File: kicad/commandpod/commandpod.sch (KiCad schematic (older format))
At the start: 3 parts

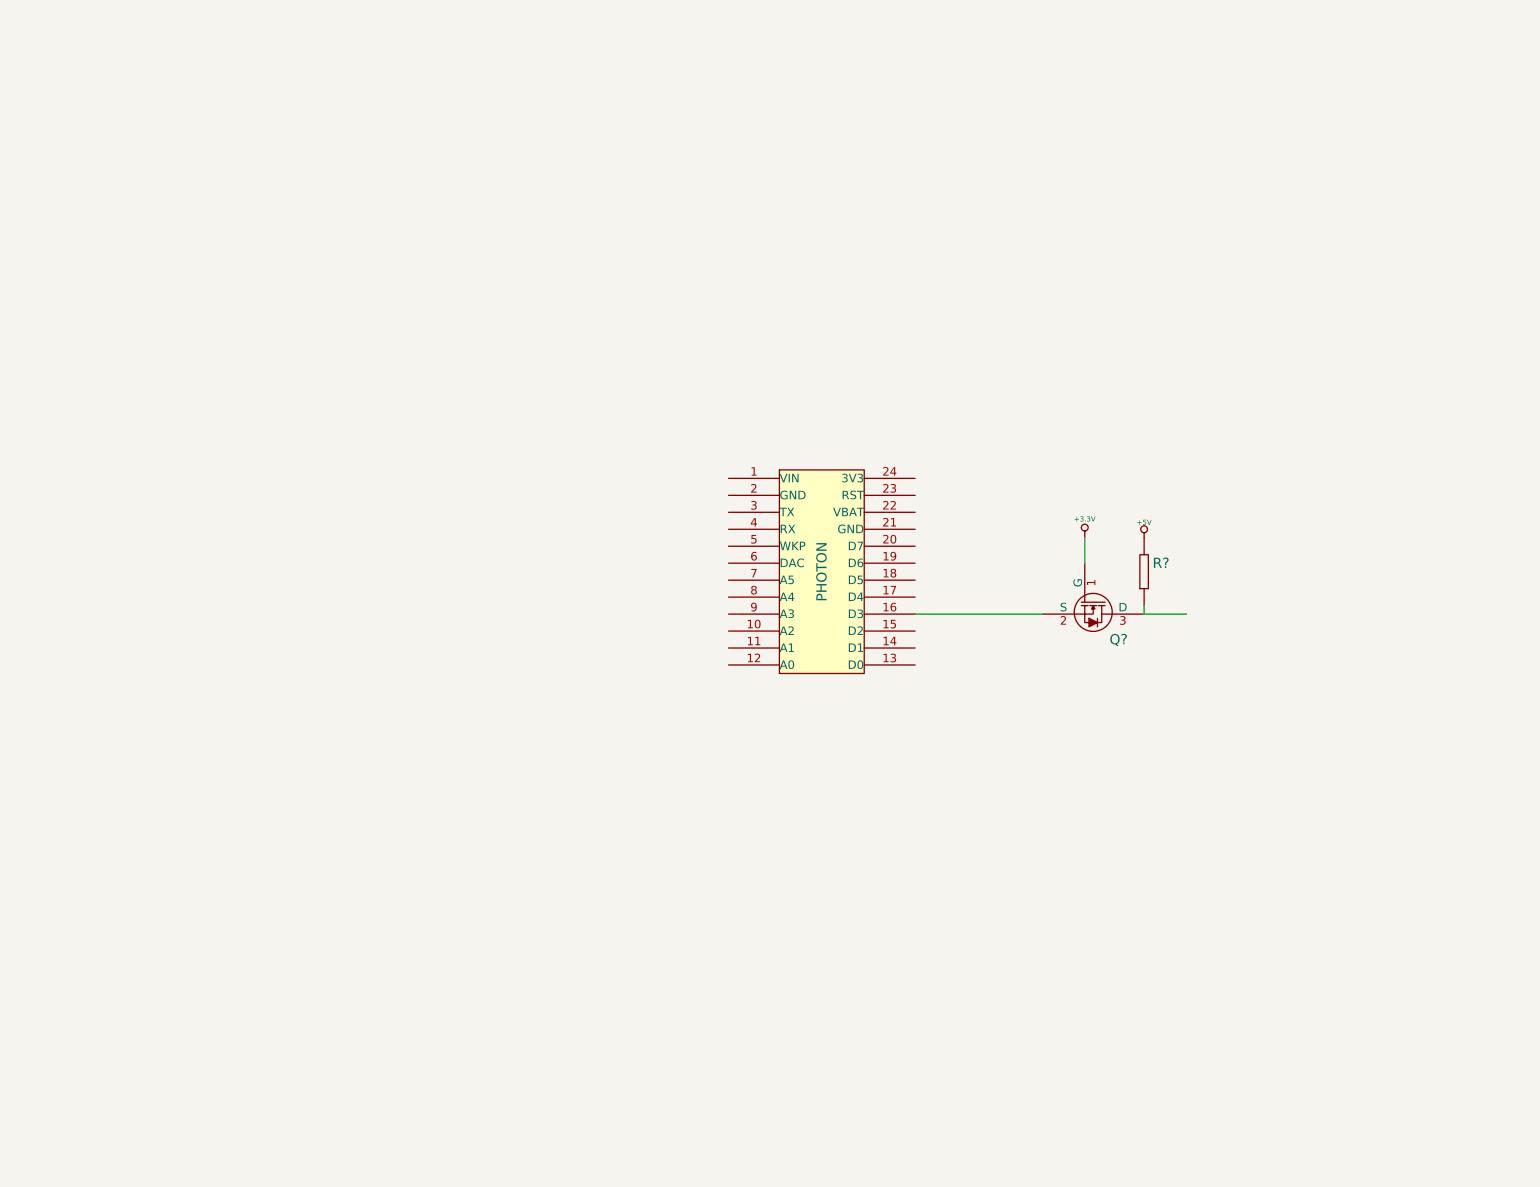
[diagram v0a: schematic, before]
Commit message: Added SPDT switch, put in ir emitter with power switch
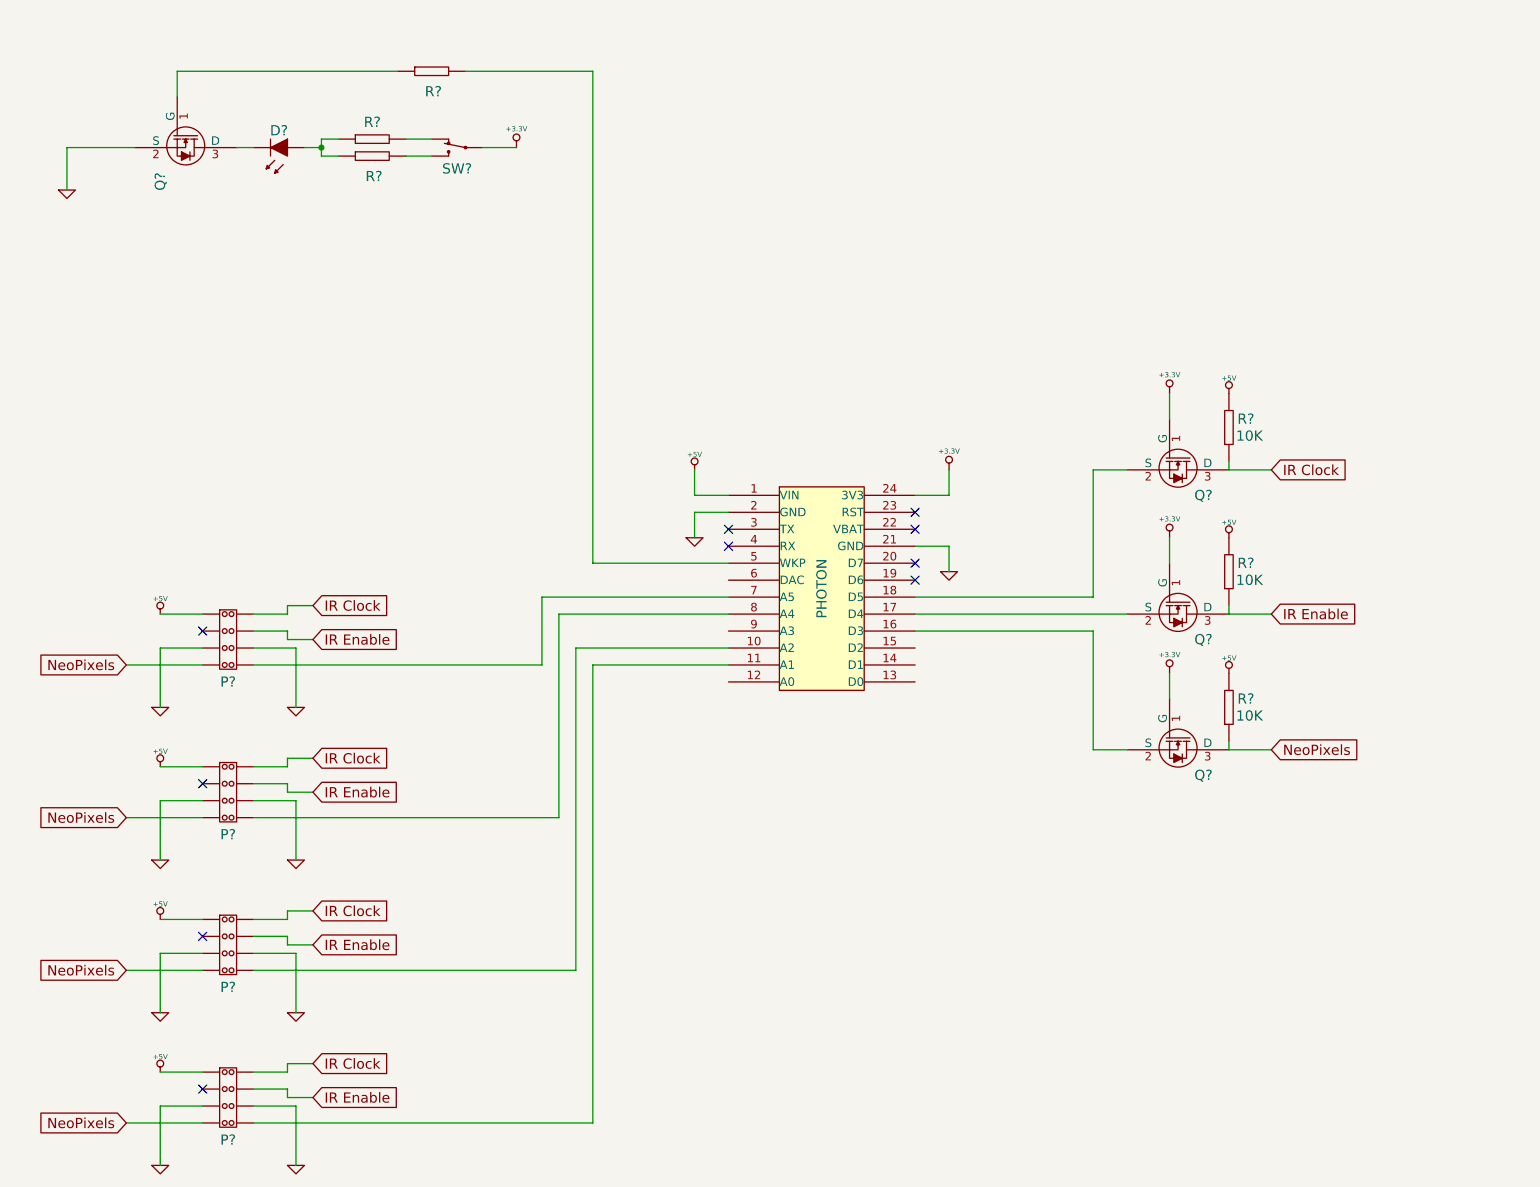
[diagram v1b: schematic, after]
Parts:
- added D?: GENERIC_LED, ~, symbol GENERIC_LED
- added P? (x4): HEADER_(8_WAY), ~, symbol HEADER_(8_WAY)
- added Q? (x3): IRFML8244TRPBF, ~, symbol IRFML8244TRPBF
- added R? (x5): GENERIC_RESISTOR, ~, symbol GENERIC_RESISTOR
- added SW?: SWITCH_SPDT, symbol SWITCH_SPDT
- R?: Resistance (none) -> 10K
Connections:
- net labels added: GND, IR Clock, IR Enable, NeoPixels
- wire segments 4 -> 99
- no-connect marks 0 -> 10
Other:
- moved on the sheet: Q?, R?

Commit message: More work on command pod
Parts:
- added B?: LM2731, ~, symbol LM2731
- added B?: BATTERY_, symbol BATTERY_
- added C? (x3): GENERIC_CAPACITOR, ~, symbol GENERIC_CAPACITOR
- added D?: SCHOTTKY_DIODE, ~, symbol SCHOTTKY_DIODE
- added L?: INDUCTOR, ~, symbol INDUCTOR
- added R?: GENERIC_RESISTOR, ~, symbol GENERIC_RESISTOR
- added R?: VARIABLE_RESISTOR, ~, symbol VARIABLE_RESISTOR
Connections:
- net +5V: now also C?.1, C?.1, D?.2, R?.2
- net GND: now also B?.2, B?.2 (GND), C?.2, C?.2, R?.1
- net at PH?.9 (A3): now also B?.4 (^SHDN), R?.1
- new net: B?.1 (SW), D?.1, L?.1
- new net: B?.3 (FB), C?.2, R?.3
- new net: B?.1, B?.5 (VIN), C?.1, L?.2, R?.2
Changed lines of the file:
@@
 Sheet 1 1
 Title ""
-Date "1 mar 2016"
+Date "2 mar 2016"
 Rev ""
 Comp ""
@@
 Wire Wire Line
 	3500 1400 3700 1400
+$Comp
+L LM2731 B?
+U 1 1 56D6D019
+P 7750 1500
+F 0 "B?" H 7550 1250 60  0000 C CNN
+F 1 "LM2731" V 7700 1500 60  0000 C CNN
+F 2 "~" H 7650 1500 60  0000 C CNN
+F 3 "~" H 7650 1500 60  0000 C CNN
+F 4 "LM2731XMF" H 7650 1350 60  0001 C CNN "Part #"
+	1    7750 1500
+	1    0    0    -1
+$EndComp
+Wire Wire Line
+	4950 4250 4250 4250
+Wire Wire Line
+	4250 4250 4250 950
+Wire Wire Line
+	4250 950  8650 950
+Wire Wire Line
+	8400 950  8400 1350
+Wire Wire Line
+	8400 1350 8200 1350
+$Comp
+L GENERIC_RESISTOR R?
+U 1 1 56D6D0A6
+P 8650 1400
+F 0 "R?" V 8700 1300 60  0000 C CNN
+F 1 "GENERIC_RESISTOR" H 8690 1180 60  0001 C CNN
+F 2 "~" H 8600 1150 60  0000 C CNN
+F 3 "~" H 8600 1150 60  0000 C CNN
+F 4 "51K" V 8600 1200 60  0000 L CNN "Resistance"
+F 5 "~" H 8860 1480 60  0001 C CNN "Part #"
+	1    8650 1400
+	0    -1   -1   0
+$EndComp
+Wire Wire Line
+	8200 1650 9150 1650
+Connection ~ 8400 950
+$Comp
+L BATTERY_ B?
+U 1 1 56D6D42D
+P 9150 1900
+F 0 "B?" V 9100 2050 60  0001 C CNN
+F 1 "BATTERY_" H 9150 2100 60  0001 C CNN
+F 2 "" H 9150 1900 60  0000 C CNN
+F 3 "" H 9150 1900 60  0000 C CNN
+F 4 "3.7-4.9V" V 9200 2150 60  0000 C CNN "Voltage"
+	1    9150 1900
+	0    1    1    0
+$EndComp
+Connection ~ 8650 1650
+$Comp
+L GENERIC_CAPACITOR C?
+U 1 1 56D6D5AB
+P 8650 1850
+F 0 "C?" V 8700 1750 60  0000 C CNN
+F 1 "GENERIC_CAPACITOR" H 8660 1650 60  0001 C CNN
+F 2 "~" H 8620 1600 60  0000 C CNN
+F 3 "~" H 8620 1600 60  0000 C CNN
+F 4 "2.2µF" V 8550 1550 60  0000 L CNN "Capacitance"
+F 5 "~" H 8960 1970 60  0001 C CNN "Part #"
+	1    8650 1850
+	0    -1   -1   0
+$EndComp
+Wire Wire Line
+	8650 2000 9150 2000
+$Comp
+L GND #PWR?
+U 1 1 56D6D772
+P 8900 2250
+F 0 "#PWR?" H 8900 2250 30  0001 C CNN
+F 1 "GND" H 8900 2180 30  0001 C CNN
+F 2 "" H 8900 2250 60  0000 C CNN
+F 3 "" H 8900 2250 60  0000 C CNN
+	1    8900 2250
+	1    0    0    -1
+$EndComp
+Wire Wire Line
+	8900 2250 8900 2000
+Connection ~ 8900 2000
+Wire Wire Line
+	6900 1500 7250 1500
+$Comp
+L SCHOTTKY_DIODE D?
+U 1 1 56D6D9AF
+P 6600 1350
+F 0 "D?" H 6600 1200 60  0000 C CNN
+F 1 "SCHOTTKY_DIODE" H 6600 1500 60  0001 C CNN
+F 2 "~" H 6600 1350 60  0000 C CNN
+F 3 "~" H 6600 1350 60  0000 C CNN
+F 4 "~" H 6700 1300 60  0001 C CNN "Part #"
+	1    6600 1350
+	-1   0    0    1
+$EndComp
+Wire Wire Line
+	6750 1350 7250 1350
+$Comp
+L +5V #PWR?
+U 1 1 56D6DA42
+P 6300 1200
+F 0 "#PWR?" H 6300 1290 20  0001 C CNN
+F 1 "+5V" H 6300 1290 30  0000 C CNN
+F 2 "" H 6300 1200 60  0000 C CNN
+F 3 "" H 6300 1200 60  0000 C CNN
+	1    6300 1200
+	1    0    0    -1
+$EndComp
+Wire Wire Line
+	6300 1200 6300 1450
+Wire Wire Line
+	5450 1350 6450 1350
+$Comp
+L INDUCTOR L?
+U 1 1 56D6DAC6
+P 7700 750
+F 0 "L?" V 7800 750 40  0000 C CNN
+F 1 "INDUCTOR" V 7800 750 40  0001 C CNN
+F 2 "~" H 7700 750 60  0000 C CNN
+F 3 "~" H 7700 750 60  0000 C CNN
+F 4 "10µH" V 7650 750 60  0000 C CNN "Inductance"
+	1    7700 750
+	0    -1   -1   0
+$EndComp
+Wire Wire Line
+	8000 750  9150 750
+Wire Wire Line
+	9150 750  9150 1800
+Wire Wire Line
+	8650 1600 8650 1700
+Wire Wire Line
+	8650 950  8650 1200
+Connection ~ 9150 1650
+Wire Wire Line
+	6900 1350 6900 750
+Wire Wire Line
+	6900 750  7400 750
+Connection ~ 6900 1350
+$Comp
+L VARIABLE_RESISTOR R?
+U 1 1 56D6DE2F
+P 6000 1800
+F 0 "R?" V 5950 1700 60  0000 C CNN
+F 1 "VARIABLE_RESISTOR" H 6040 1580 60  0001 C CNN
+F 2 "~" H 5950 1550 60  0000 C CNN
+F 3 "~" H 5950 1550 60  0000 C CNN
+F 4 "100K" V 6050 1650 60  0000 C CNN "Resistance"
+F 5 "~" H 6210 1880 60  0001 C CNN "Part #"
+	1    6000 1800
+	0    1    1    0
+$EndComp
+Wire Wire Line
+	6000 1350 6000 1600
+Connection ~ 6300 1350
+$Comp
+L GND #PWR?
+U 1 1 56D6E012
+P 6000 2250
+F 0 "#PWR?" H 6000 2250 30  0001 C CNN
+F 1 "GND" H 6000 2180 30  0001 C CNN
+F 2 "" H 6000 2250 60  0000 C CNN
+F 3 "" H 6000 2250 60  0000 C CNN
+	1    6000 2250
+	1    0    0    -1
+$EndComp
+$Comp
+L GENERIC_CAPACITOR C?
+U 1 1 56D6E0A1
+P 5450 1800
+F 0 "C?" V 5500 1900 60  0000 C CNN
+F 1 "GENERIC_CAPACITOR" H 5460 1600 60  0001 C CNN
+F 2 "~" H 5420 1550 60  0000 C CNN
+F 3 "~" H 5420 1550 60  0000 C CNN
+F 4 "4.7µF" V 5350 1950 60  0000 C CNN "Capacitance"
+F 5 "~" H 5760 1920 60  0001 C CNN "Part #"
+	1    5450 1800
+	0    -1   -1   0
+$EndComp
+Wire Wire Line
+	5450 1350 5450 1650
+Connection ~ 6000 1350
+Wire Wire Line
+	5450 2050 6900 2050
+Connection ~ 6000 2050
+Wire Wire Line
+	6900 2050 6900 1500
+$Comp
+L GENERIC_CAPACITOR C?
+U 1 1 56D6E31F
+P 6300 1600
+F 0 "C?" V 6350 1500 60  0000 C CNN
+F 1 "GENERIC_CAPACITOR" H 6310 1400 60  0001 C CNN
+F 2 "~" H 6270 1350 60  0000 C CNN
+F 3 "~" H 6270 1350 60  0000 C CNN
+F 4 "220pF" V 6200 1300 60  0000 L CNN "Capacitance"
+F 5 "~" H 6610 1720 60  0001 C CNN "Part #"
+	1    6300 1600
+	0    -1   -1   0
+$EndComp
+Wire Wire Line
+	6150 1800 6700 1800
+Wire Wire Line
+	6300 1800 6300 1750
+Wire Wire Line
+	6700 1650 7250 1650
+Connection ~ 6300 1800
+Wire Wire Line
+	5450 2050 5450 1950
+Wire Wire Line
+	6000 2000 6000 2250
+Wire Wire Line
+	6700 1800 6700 1650
 $EndSCHEMATC

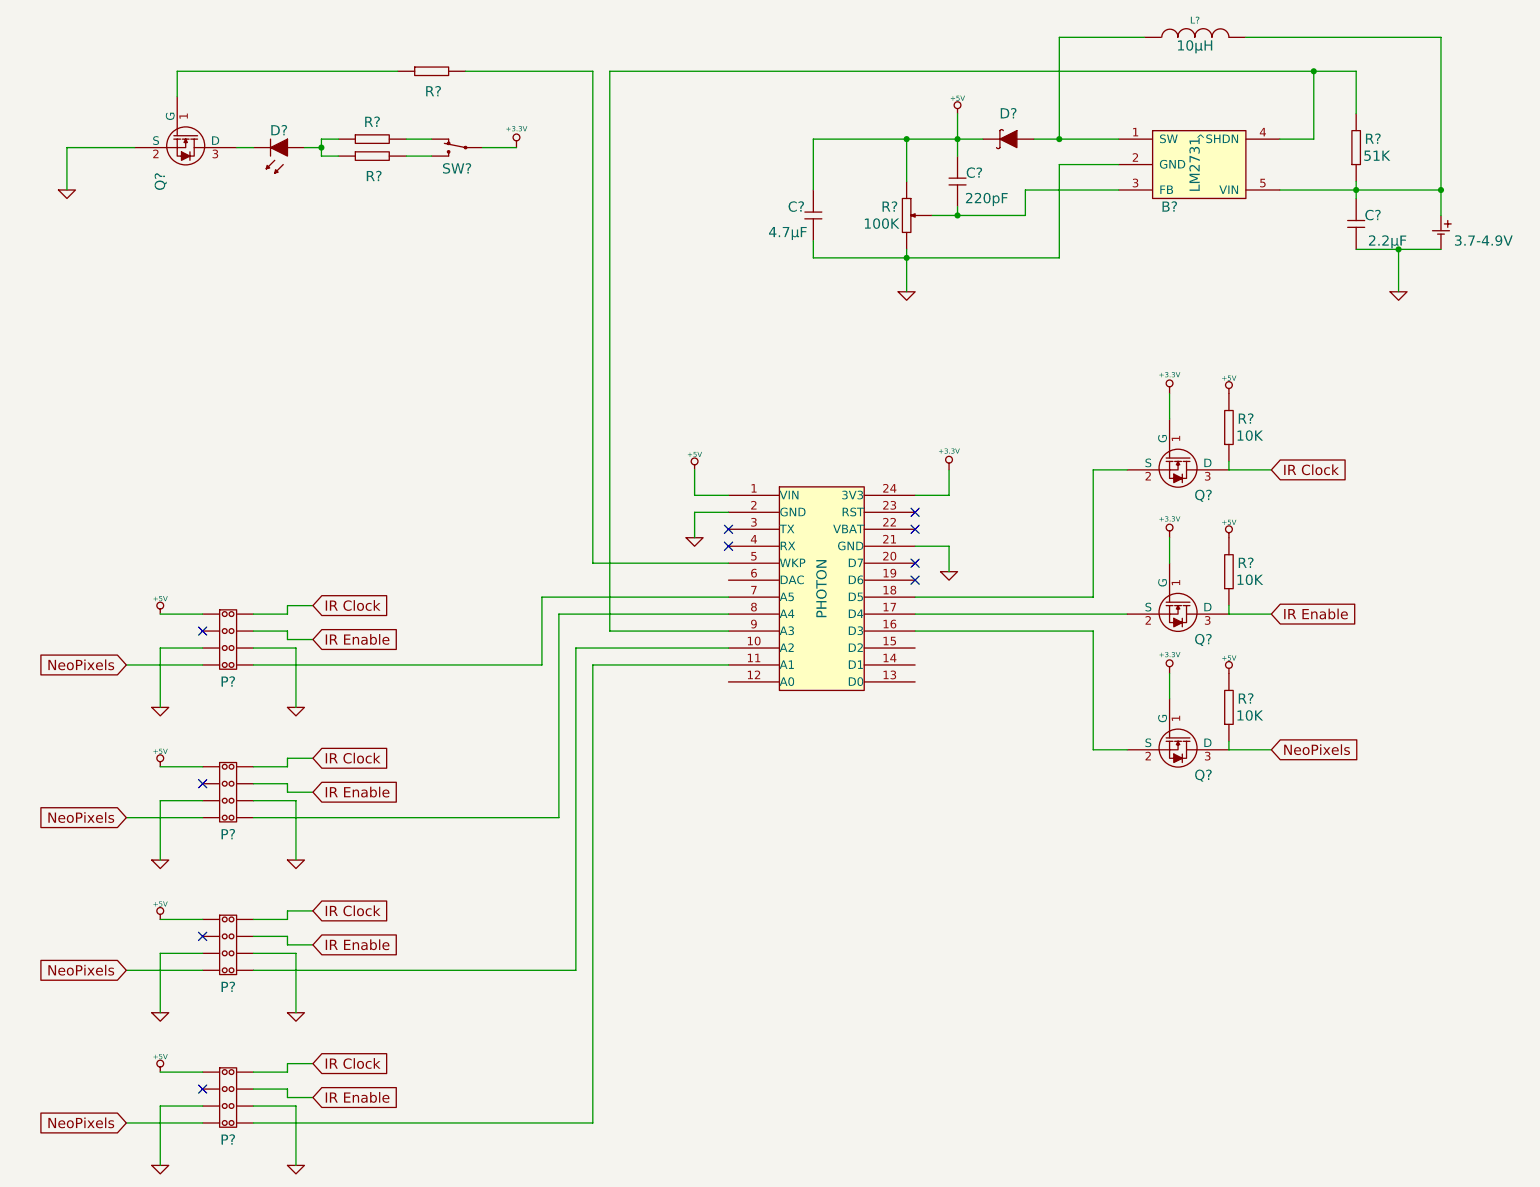
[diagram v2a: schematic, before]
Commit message: Added heirarchial schematics for command pod
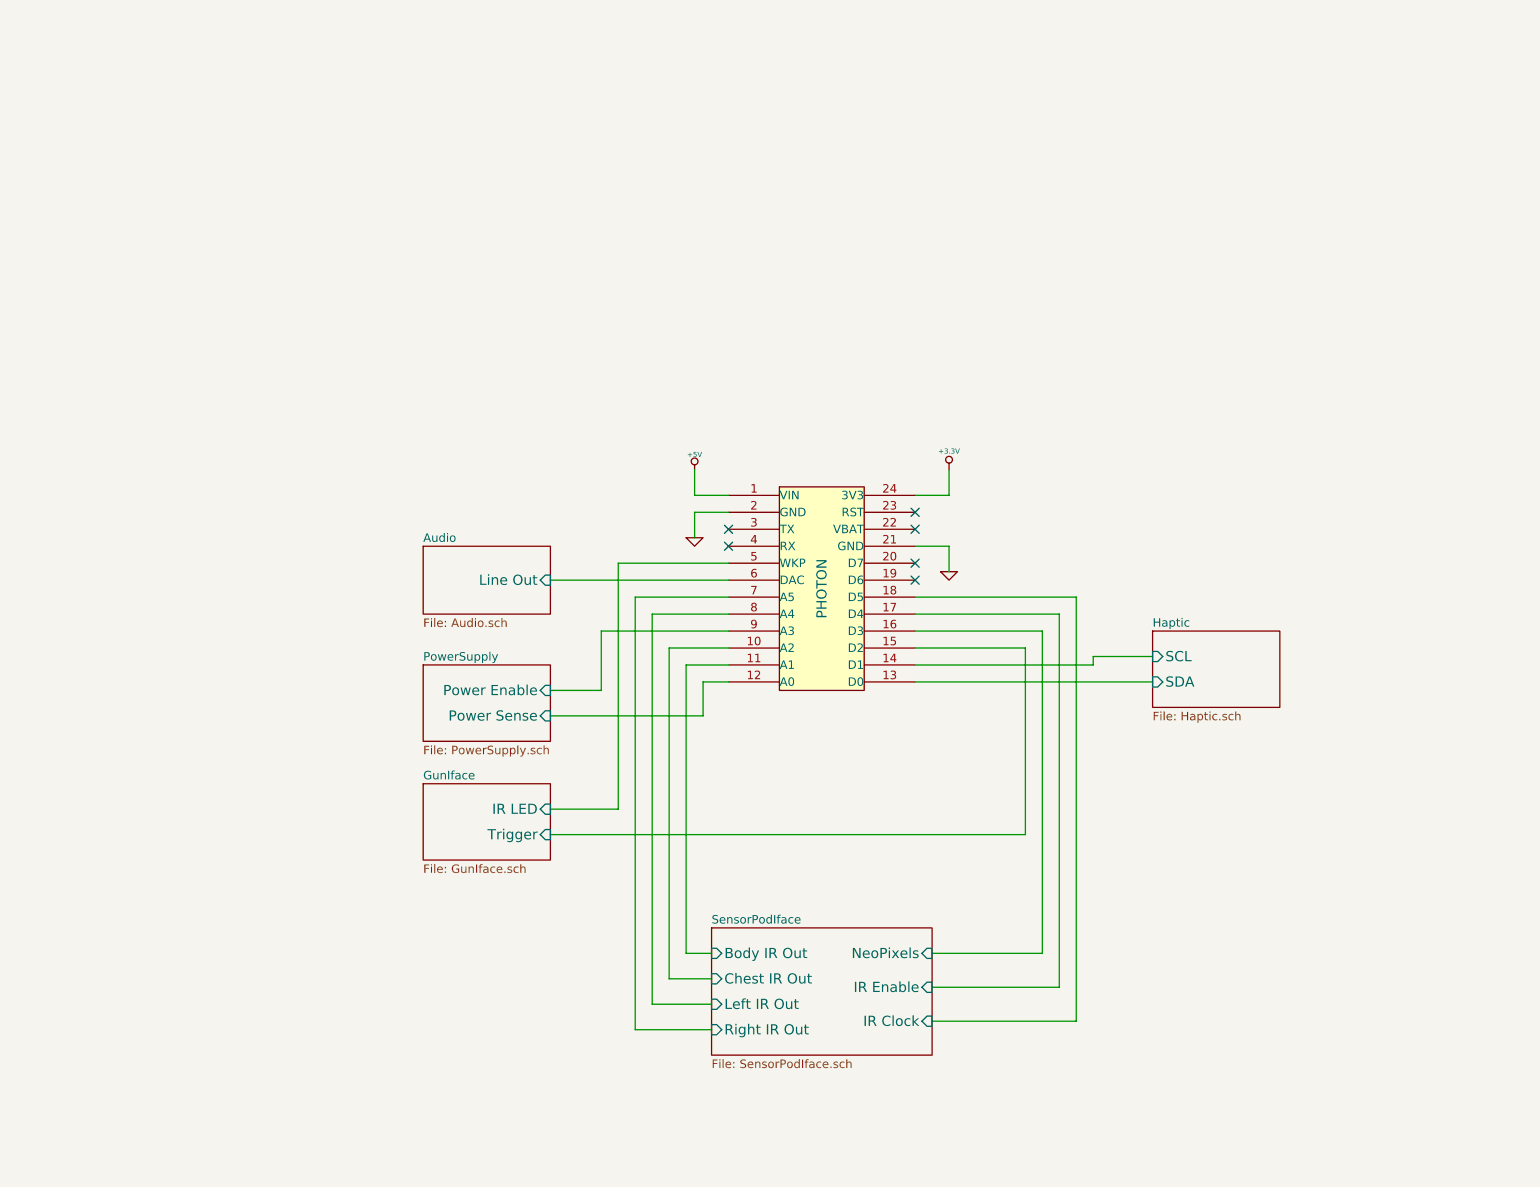
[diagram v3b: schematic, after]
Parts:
- removed B?: LM2731, ~, symbol LM2731
- removed B?: BATTERY_, symbol BATTERY_
- removed C? (x3): GENERIC_CAPACITOR, ~, symbol GENERIC_CAPACITOR
- removed D?: GENERIC_LED, ~, symbol GENERIC_LED
- removed D?: SCHOTTKY_DIODE, ~, symbol SCHOTTKY_DIODE
- removed L?: INDUCTOR, ~, symbol INDUCTOR
- removed P? (x4): HEADER_(8_WAY), ~, symbol HEADER_(8_WAY)
- removed Q? (x4): IRFML8244TRPBF, ~, symbol IRFML8244TRPBF
- removed R? (x7): GENERIC_RESISTOR, ~, symbol GENERIC_RESISTOR
- removed R?: VARIABLE_RESISTOR, ~, symbol VARIABLE_RESISTOR
- removed SW?: SWITCH_SPDT, symbol SWITCH_SPDT
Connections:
- net SensorPodIface/Chest IR Out: now reaches PH?.10 (A2)
- net SensorPodIface/Body IR Out: now reaches PH?.11 (A1)
- net PowerSupply/Power Sense: now reaches PH?.12 (A0)
- net Haptic/SDA: now reaches PH?.13 (D0)
- net Haptic/SCL: now reaches PH?.14 (D1)
- net GunIface/Trigger: now reaches PH?.15 (D2)
- net SensorPodIface/NeoPixels: now reaches PH?.16 (D3)
- net SensorPodIface/IR Enable: now reaches PH?.17 (D4)
- net SensorPodIface/IR Clock: now reaches PH?.18 (D5)
- net GunIface/IR LED: now reaches PH?.5 (WKP)
- net Audio/Line Out: now reaches PH?.6 (DAC)
- net SensorPodIface/Right IR Out: now reaches PH?.7 (A5)
- net SensorPodIface/Left IR Out: now reaches PH?.8 (A4)
- net PowerSupply/Power Enable: now reaches PH?.9 (A3)
- no-connect marks 10 -> 6
